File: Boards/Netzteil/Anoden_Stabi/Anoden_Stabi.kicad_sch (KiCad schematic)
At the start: 24 parts, among them J1 Conn_01x06, P1 CONN_3, Q1 2SC2979, Q2 MJE5731

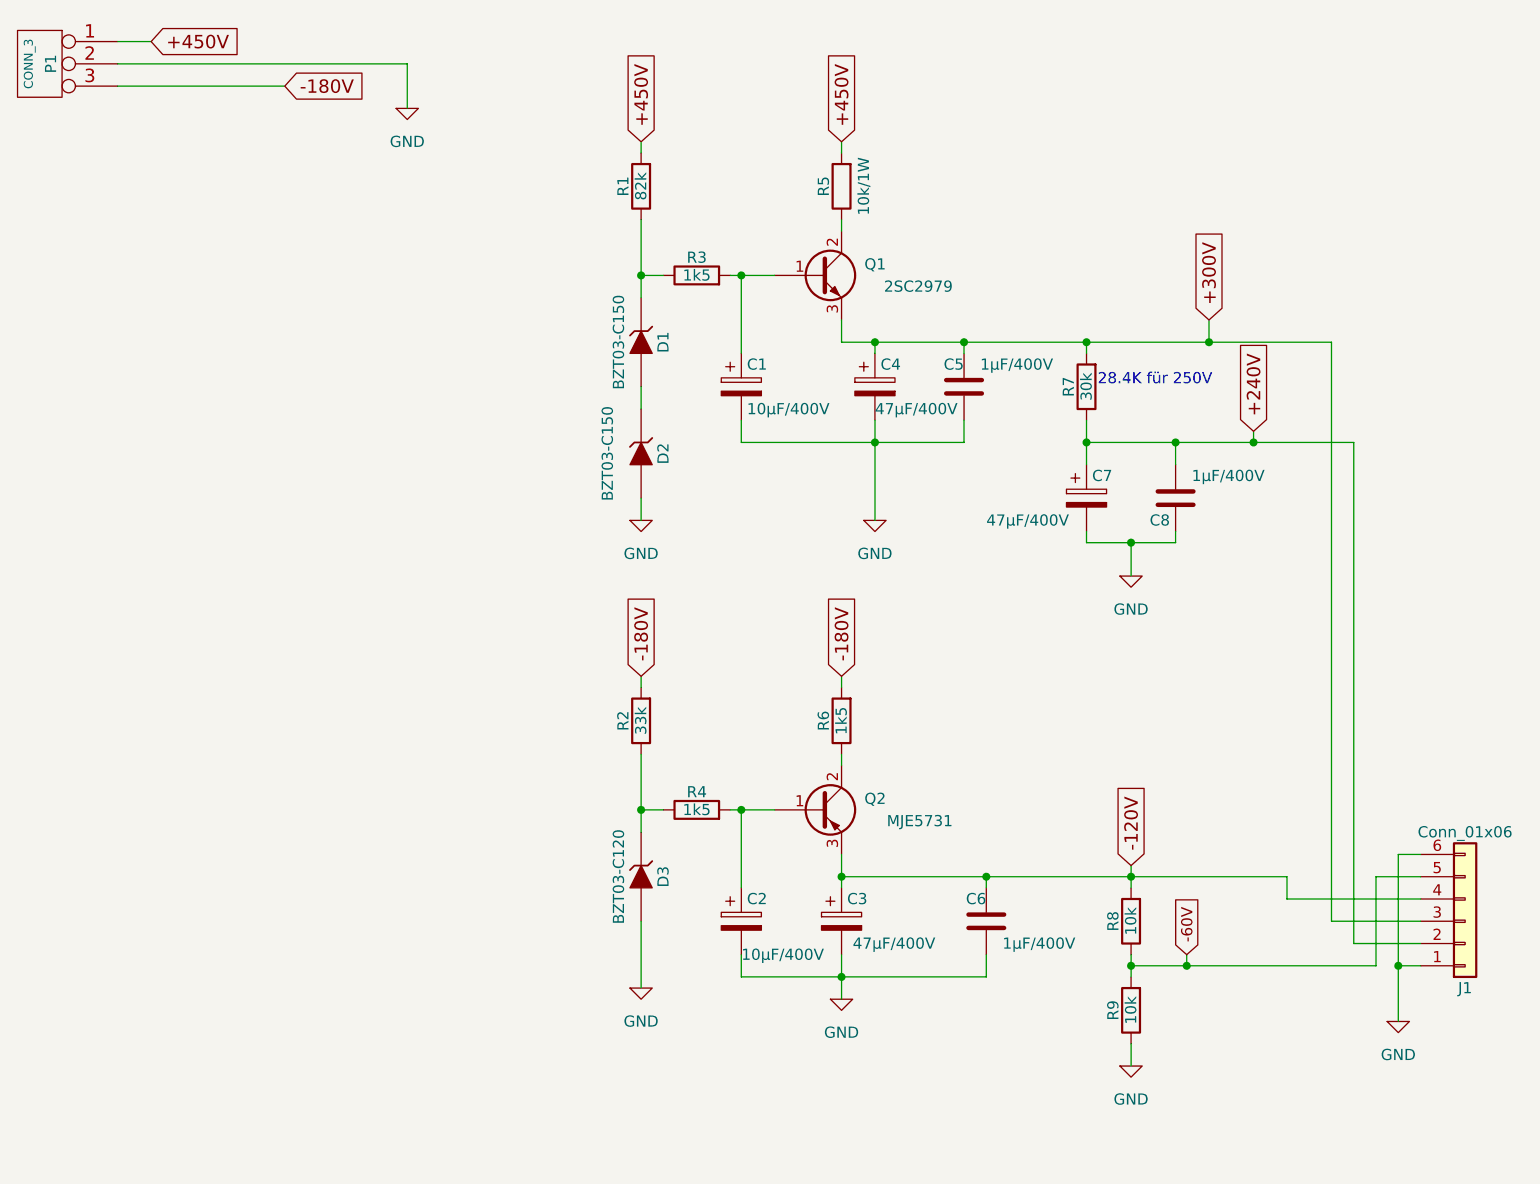
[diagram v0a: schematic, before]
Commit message: 6.3V, 400V und 400V Regler Boards bestellt
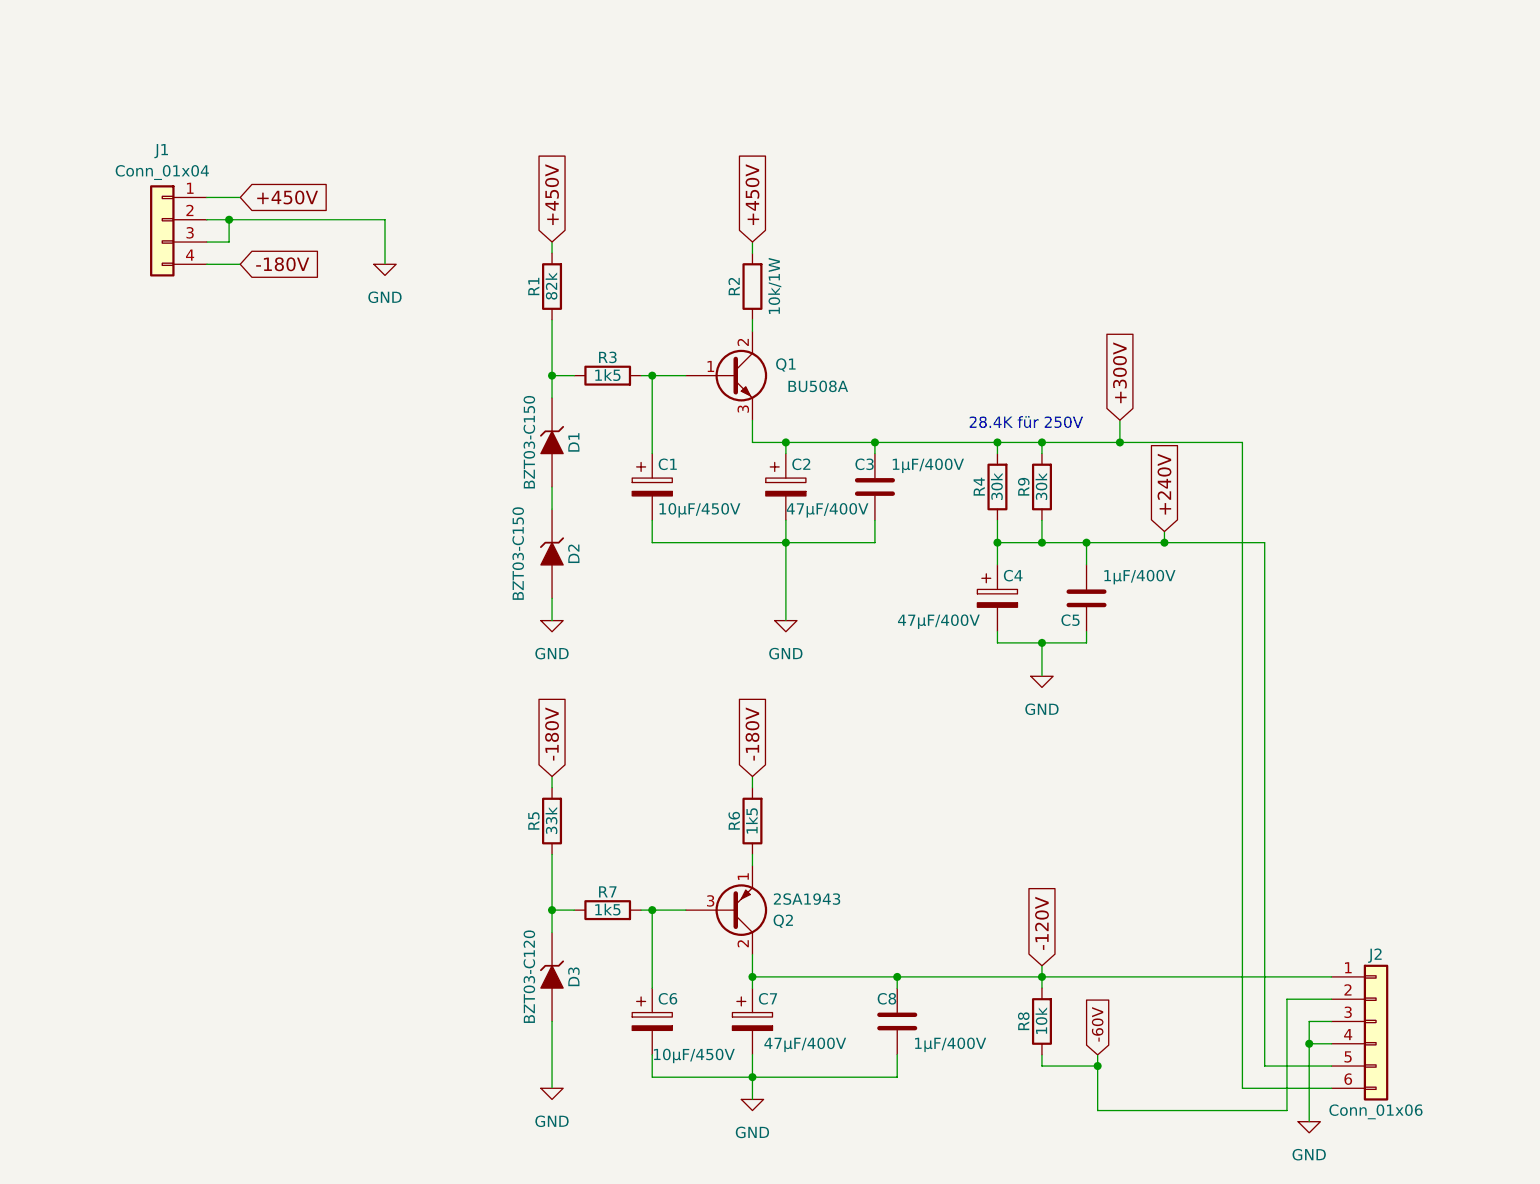
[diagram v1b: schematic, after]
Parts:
- removed P1: CONN_3, Connectors_Mini-Universal:MiniUniversalMate-N-LokSocket_3PinVertical, symbol Anoden_Stabi-rescue:CONN_3-borniers
- removed Q2: MJE5731, Package_TO_SOT_THT:TO-220-3_Vertical, symbol Device:Q_PNP_BCE
- added J1: Conn_01x04, Connector_Molex:Molex_Mini-Fit_Jr_5566-04A_2x02_P4.20mm_Vertical, symbol Connector_Generic:Conn_01x04
- added Q2: 2SA1943, Package_TO_SOT_THT:TO-3P-3_Vertical, symbol Device:Q_PNP_ECB
- C1: value 10µF/400V -> 10µF/450V; footprint Capacitor_THT:CP_Radial_D10.0mm_P5.00mm -> Capacitor_THT:CP_Radial_D12.5mm_P5.00mm
- C2: renamed from C4; footprint Capacitor_THT:CP_Radial_D16.0mm_P7.50mm -> Capacitor_THT:CP_Radial_D22.0mm_P10.00mm_SnapIn
- C4: renamed from C7; footprint Capacitor_THT:CP_Radial_D16.0mm_P7.50mm -> Capacitor_THT:CP_Radial_D22.0mm_P10.00mm_SnapIn
- C6: renamed from C2; value 10µF/400V -> 10µF/450V; footprint Capacitor_THT:CP_Radial_D10.0mm_P5.00mm -> Capacitor_THT:CP_Radial_D12.5mm_P5.00mm
- C7: renamed from C3; footprint Capacitor_THT:CP_Radial_D16.0mm_P7.50mm -> Capacitor_THT:CP_Radial_D22.0mm_P10.00mm_SnapIn
- J2: renamed from J1; footprint Connectors_Mini-Universal:MiniUniversalMate-N-LokSocket_6PinVertical -> Connector_Molex:Molex_Mini-Fit_Jr_5566-06A_2x03_P4.20mm_Vertical
- Q1: value 2SC2979 -> BU508A; footprint Package_TO_SOT_THT:TO-220-3_Vertical -> Package_TO_SOT_THT:TO-3P-3_Vertical
- R2: renamed from R5; footprint Resistor_THT:R_Axial_DIN0207_L6.3mm_D2.5mm_P10.16mm_Horizontal -> Resistor_THT:R_Axial_DIN0414_L11.9mm_D4.5mm_P15.24mm_Horizontal
- R3, R6, R8: footprint Resistor_THT:R_Axial_DIN0207_L6.3mm_D2.5mm_P10.16mm_Horizontal -> Resistor_THT:R_Axial_DIN0414_L11.9mm_D4.5mm_P15.24mm_Horizontal
- R7: renamed from R4; footprint Resistor_THT:R_Axial_DIN0207_L6.3mm_D2.5mm_P10.16mm_Horizontal -> Resistor_THT:R_Axial_DIN0414_L11.9mm_D4.5mm_P15.24mm_Horizontal
- R9: value 10k -> 30k
- renumbered C5 to C3, C8 to C5, C6 to C8, R7 to R4, R2 to R5
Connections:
- net +240V: now also J2.5 (Pin_5), R9.1; no longer J2.2 (Pin_2)
- net +300V: now also J2.6 (Pin_6), R9.2; no longer J2.3 (Pin_3)
- net +450V: now also J1.1 (Pin_1)
- net -120V: now also J2.1 (Pin_1), Q2.2 (C); no longer J2.4 (Pin_4)
- net -180V: now also J1.4 (Pin_4)
- net -60V: now also J2.2 (Pin_2); no longer J2.5 (Pin_5), R9.2
- net GND: now also J2.3 (Pin_3), J2.4 (Pin_4), J1.2 (Pin_2), J1.3 (Pin_3); no longer J2.1 (Pin_1), J2.6 (Pin_6), R9.1
- net at C6.1, R7.2: now also Q2.3 (B)
- net at R6.1: now also Q2.1 (E)
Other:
- moved on the sheet: C1, C2, C3, C4, C5, C6, C7, C8, D1, D2, D3, J2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

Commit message: Leiterplatte erstellt
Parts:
- C2, C4, C7: footprint Capacitor_THT:CP_Radial_D22.0mm_P10.00mm_SnapIn -> Capacitor_THT:CP_Radial_D17.0mm_P7.50mm
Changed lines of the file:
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@@
 			)
 		)
-		(property "Footprint" "Capacitor_THT:CP_Radial_D22.0mm_P10.00mm_SnapIn"
+		(property "Footprint" "Capacitor_THT:CP_Radial_D17.0mm_P7.50mm"
 			(at 131.7752 83.82 0)
 			(effects
@@
 			)
 		)
-		(property "Footprint" "Capacitor_THT:CP_Radial_D22.0mm_P10.00mm_SnapIn"
+		(property "Footprint" "Capacitor_THT:CP_Radial_D17.0mm_P7.50mm"
 			(at 155.9052 96.52 0)
 			(effects
@@
 			)
 		)
-		(property "Footprint" "Capacitor_THT:CP_Radial_D22.0mm_P10.00mm_SnapIn"
+		(property "Footprint" "Capacitor_THT:CP_Radial_D17.0mm_P7.50mm"
 			(at 127.9652 144.78 0)
 			(effects
